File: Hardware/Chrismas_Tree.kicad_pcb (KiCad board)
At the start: 2 copper layers, 264.4 x 368.3 mm, 213 parts, among them J1 DNP, J2 USB_B, Q1 2N2222A, Q2 2N2222A, Q3 2N2222A, Q4 2N2222A, U1 PIC18F23K22

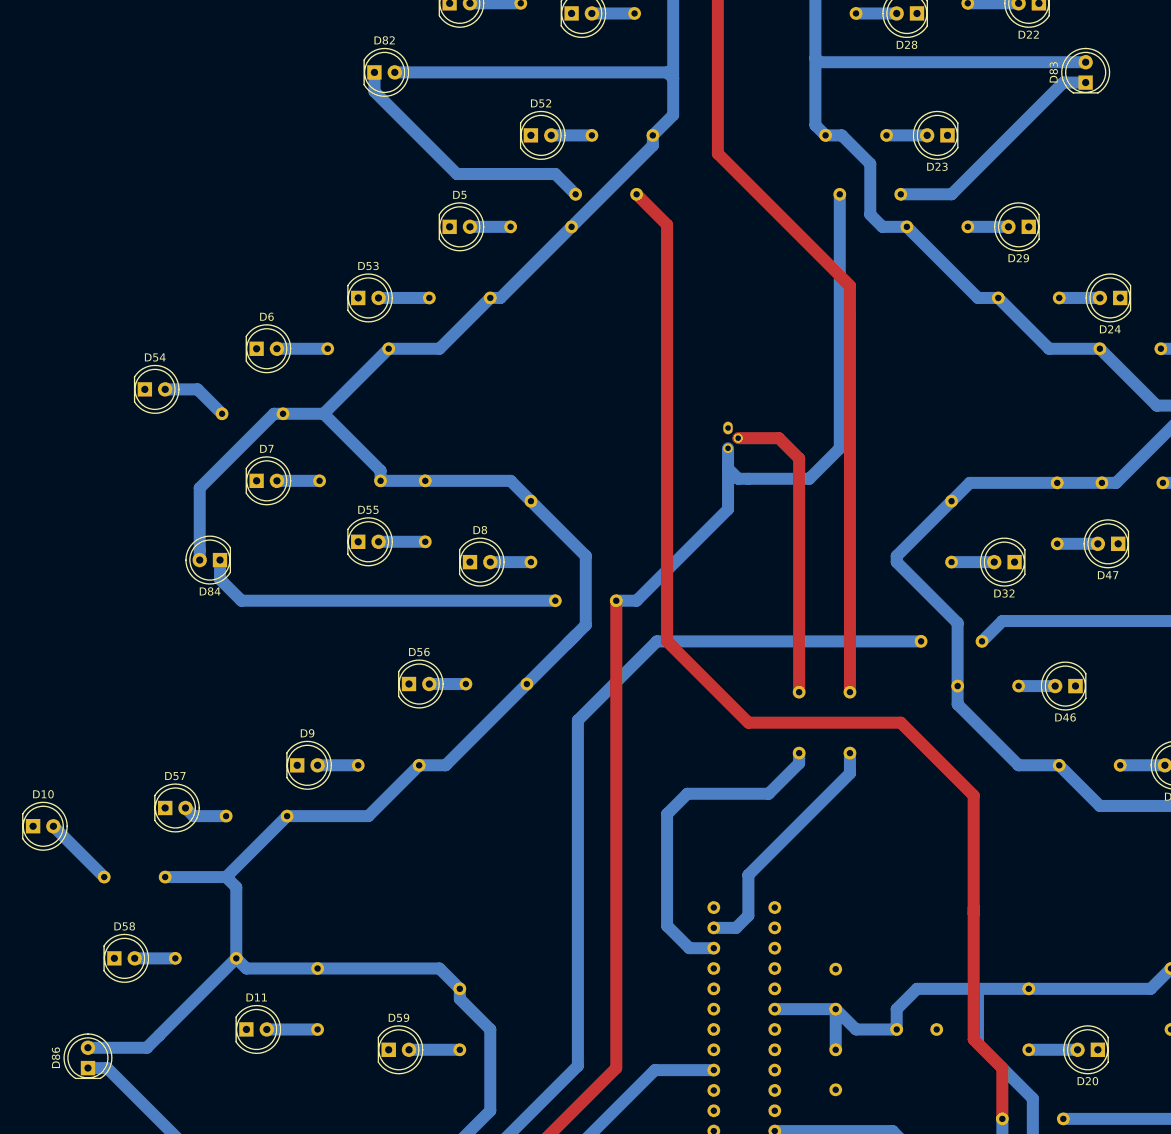
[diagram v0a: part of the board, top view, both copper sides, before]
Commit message: Turned rotated leds to have all them on the same axis (but trunk base ones).
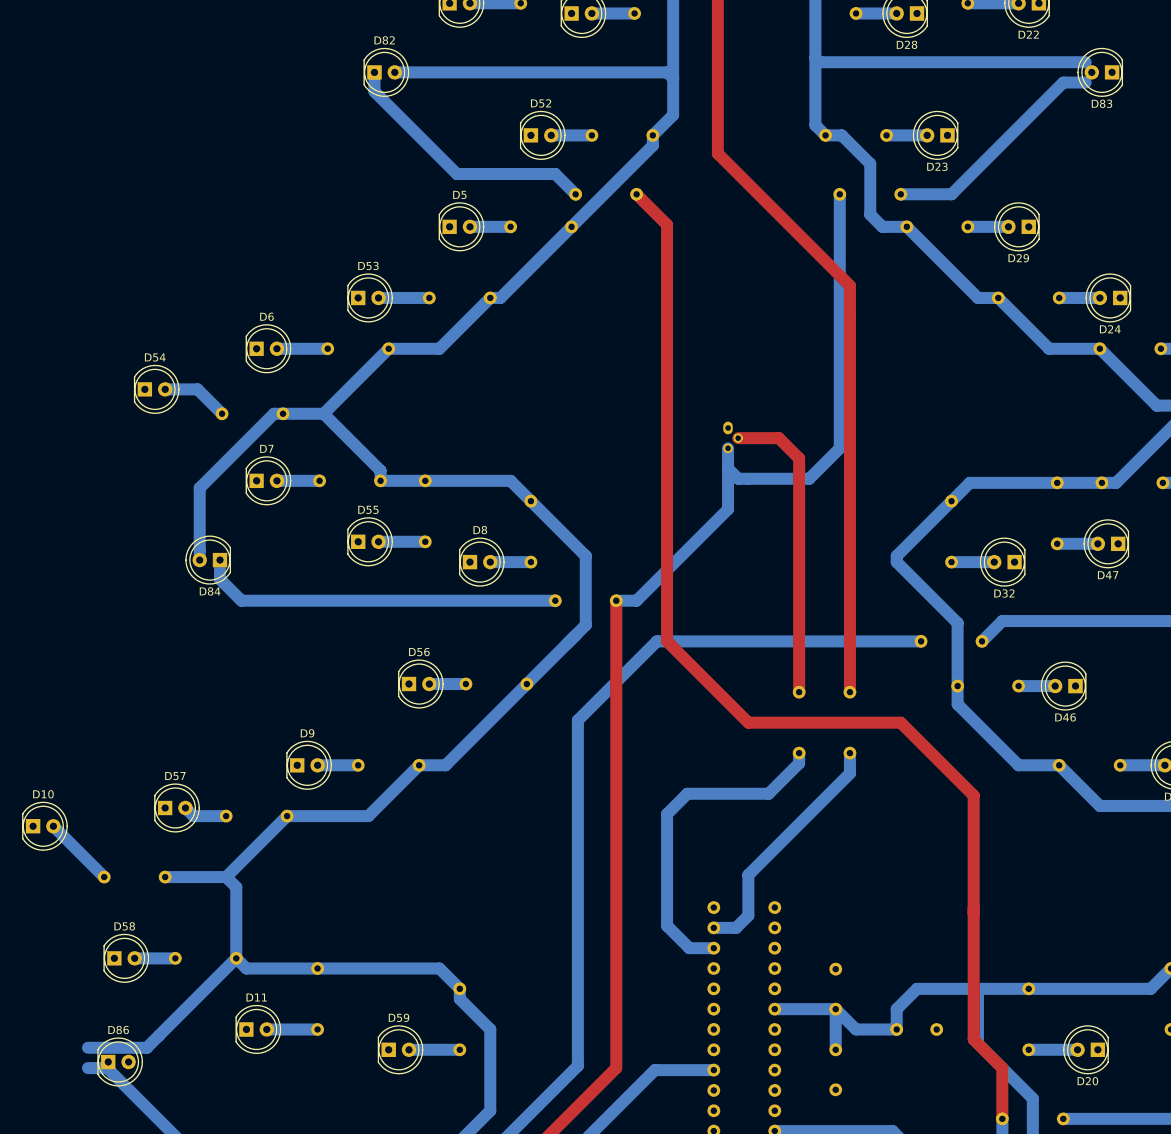
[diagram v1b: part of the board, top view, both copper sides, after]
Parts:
- moved D83 3.54 mm to (208.0, 127.0), turned to 180 degrees
- moved D86 2.65 mm to (82.5, 250.7), turned to 0 degrees
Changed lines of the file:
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@@
   (general
     (thickness 1.6)
-    (drawings 7)
+    (drawings 8)
     (tracks 514)
     (zones 0)
@@
   )
   (module LED_THT:LED_D5.0mm (layer F.Cu)
-    (at 80.01 251.46 90)
+    (at 82.55 250.698)
     (descr "LED, diameter 5.0mm, 2 pins, http://cdn-reichelt.de/documents/datenblatt/A500/LL-504BC2E-009.pdf")
     (tags "LED diameter 5.0mm 2 pins")
-    (fp_text reference D86 (at 1.27 -3.96 90) (layer F.SilkS)
+    (fp_text reference D86 (at 1.27 -3.96) (layer F.SilkS)
       (effects (font (size 1 1) (thickness 0.15)))
     )
-    (fp_text value Yellow (at 1.27 3.96 90) (layer F.Fab)
+    (fp_text value Yellow (at 1.27 3.96) (layer F.Fab)
       (effects (font (size 1 1) (thickness 0.15)))
     )
-    (fp_text user %R (at 1.25 0 90) (layer F.Fab)
+    (fp_text user %R (at 1.25 0) (layer F.Fab)
       (effects (font (size 0.8 0.8) (thickness 0.2)))
     )
@@
     (fp_arc (start 1.27 0) (end -1.29 -1.54483) (angle 148.9) (layer F.SilkS) (width 0.12))
     (fp_arc (start 1.27 0) (end -1.23 -1.469694) (angle 299.1) (layer F.Fab) (width 0.1))
-    (pad 2 thru_hole circle (at 2.54 0 90) (size 1.8 1.8) (drill 0.9) (layers *.Cu *.Mask)
+    (pad 2 thru_hole circle (at 2.54 0) (size 1.8 1.8) (drill 0.9) (layers *.Cu *.Mask)
       (net 83 +5V))
-    (pad 1 thru_hole rect (at 0 0 90) (size 1.8 1.8) (drill 0.9) (layers *.Cu *.Mask)
+    (pad 1 thru_hole rect (at 0 0) (size 1.8 1.8) (drill 0.9) (layers *.Cu *.Mask)
       (net 110 "Net-(D86-Pad1)"))
     (model ${KISYS3DMOD}/LED_THT.3dshapes/LED_D5.0mm.wrl
@@
   )
   (module LED_THT:LED_D5.0mm (layer F.Cu)
-    (at 204.724 128.27 90)
+    (at 208.026 127 180)
     (descr "LED, diameter 5.0mm, 2 pins, http://cdn-reichelt.de/documents/datenblatt/A500/LL-504BC2E-009.pdf")
     (tags "LED diameter 5.0mm 2 pins")
-    (fp_text reference D83 (at 1.27 -3.96 90) (layer F.SilkS)
+    (fp_text reference D83 (at 1.27 -3.96) (layer F.SilkS)
       (effects (font (size 1 1) (thickness 0.15)))
     )
-    (fp_text value Red (at 1.27 3.96 90) (layer F.Fab)
+    (fp_text value Red (at 1.27 3.96) (layer F.Fab)
       (effects (font (size 1 1) (thickness 0.15)))
     )
-    (fp_text user %R (at 1.25 0 90) (layer F.Fab)
+    (fp_text user %R (at 1.25 0) (layer F.Fab)
       (effects (font (size 0.8 0.8) (thickness 0.2)))
     )
@@
     (fp_arc (start 1.27 0) (end -1.29 -1.54483) (angle 148.9) (layer F.SilkS) (width 0.12))
     (fp_arc (start 1.27 0) (end -1.23 -1.469694) (angle 299.1) (layer F.Fab) (width 0.1))
-    (pad 2 thru_hole circle (at 2.54 0 90) (size 1.8 1.8) (drill 0.9) (layers *.Cu *.Mask)
+    (pad 2 thru_hole circle (at 2.54 0 180) (size 1.8 1.8) (drill 0.9) (layers *.Cu *.Mask)
       (net 83 +5V))
-    (pad 1 thru_hole rect (at 0 0 90) (size 1.8 1.8) (drill 0.9) (layers *.Cu *.Mask)
+    (pad 1 thru_hole rect (at 0 0 180) (size 1.8 1.8) (drill 0.9) (layers *.Cu *.Mask)
       (net 107 "Net-(D83-Pad1)"))
     (model ${KISYS3DMOD}/LED_THT.3dshapes/LED_D5.0mm.wrl
@@
     )
   )
+  (dimension 131 (width 0.12) (layer F.SilkS)
+    (gr_text "131,000 mm" (at 227.45 24.34) (layer F.SilkS)
+      (effects (font (size 1 1) (thickness 0.15)))
+    )
+    (feature1 (pts (xy 292.95 384.61) (xy 292.95 25.023579)))
+    (feature2 (pts (xy 161.95 384.61) (xy 161.95 25.023579)))
+    (crossbar (pts (xy 161.95 25.61) (xy 292.95 25.61)))
+    (arrow1a (pts (xy 292.95 25.61) (xy 291.823496 26.196421)))
+    (arrow1b (pts (xy 292.95 25.61) (xy 291.823496 25.023579)))
+    (arrow2a (pts (xy 161.95 25.61) (xy 163.076504 26.196421)))
+    (arrow2b (pts (xy 161.95 25.61) (xy 163.076504 25.023579)))
+  )
   (gr_text 11/2019 (at 262.89 388.62) (layer F.Mask)
     (effects (font (size 1 1) (thickness 0.15)))
@@
     (polygon
       (pts
-        (xy 28.702 25.654) (xy 293.116 25.654) (xy 293.116 393.954) (xy 28.702 393.954)
+        (xy 293.116 393.954) (xy 28.702 393.954) (xy 28.702 25.654) (xy 293.116 25.654)
       )
     )

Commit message: Replaced tree foliage through-hole resistors by SMD ones.
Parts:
- R1, R10, R11, R12, R13, R14, R15, R16, R17, R18, R19, R2, R20, R21, R22, R23, R24, R25, R26, R27, R28, R29, R3, R30, R31, R32, R33, R34, R35, R36, R37, R38, R39, R4, R40, R41, R42, R43, R44, R45, R46, R47, R48, R49, R5, R50, R51, R52, R53, R54, R55, R56, R57, R58, R59, R6, R60, R61, R62, R63, R64, R65, R66, R67, R68, R7, R8, R9: footprint Resistor_THT:R_Axial_DIN0207_L6.3mm_D2.5mm_P7.62mm_Horizontal -> Resistor_SMD:R_1206_3216Metric_Pad1.42x1.75mm_HandSolder
- moved R10 9.95 mm to (82.0, 221.2)
- moved R34 9.59 mm to (241.8, 221.5)
- moved R54 8.95 mm to (96.0, 166.6)
- moved R48 8.62 mm to (226.6, 166.6)
- moved R62 8.10 mm to (275.9, 292.4)
- moved R38 7.88 mm to (45.9, 292.4)
- moved R8 7.69 mm to (136.4, 188.2), turned to 180 degrees
- moved R32 7.66 mm to (187.2, 188.2), turned to 0 degrees
- moved R28 7.66 mm to (175.3, 119.6), turned to 0 degrees
- moved R12 7.66 mm to (115.0, 264.4)
- moved R59 7.63 mm to (126.2, 249.2), turned to 180 degrees
- moved R4 7.62 mm to (148.6, 119.6), turned to 180 degrees
- moved R20 7.62 mm to (197.6, 249.2), turned to 0 degrees
- moved R36 7.40 mm to (208.8, 264.4)
- moved R53 7.40 mm to (122.9, 155.2)
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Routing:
- net +5V: track 1804.1 -> 2168.2 mm
- net Net-(D83-Pad1): track 28.9 -> 34.1 mm
- net Net-(D10-Pad2): track 8.98 -> 4.83 mm
- net Net-(D34-Pad2): track 8.41 -> 4.32 mm
- net Net-(D54-Pad2): track 8.37 -> 4.83 mm
- net Net-(D48-Pad2): track 8.21 -> 5.12 mm
- net Net-(D62-Pad2): track 7.67 -> 5.08 mm
- net Net-(D38-Pad2): track 7.42 -> 5.08 mm
- net Net-(D59-Pad2): track 6.35 -> 4.57 mm
- net Net-(D20-Pad2): track 6.10 -> 4.57 mm
- net Net-(D12-Pad2): track 5.84 -> 4.32 mm
- net Net-(D45-Pad2): track 5.75 -> 4.39 mm
- net Net-(D4-Pad2): track 5.33 -> 4.06 mm
- net Net-(D53-Pad2): track 6.35 -> 5.08 mm
- net Net-(D37-Pad2): track 6.35 -> 5.33 mm
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
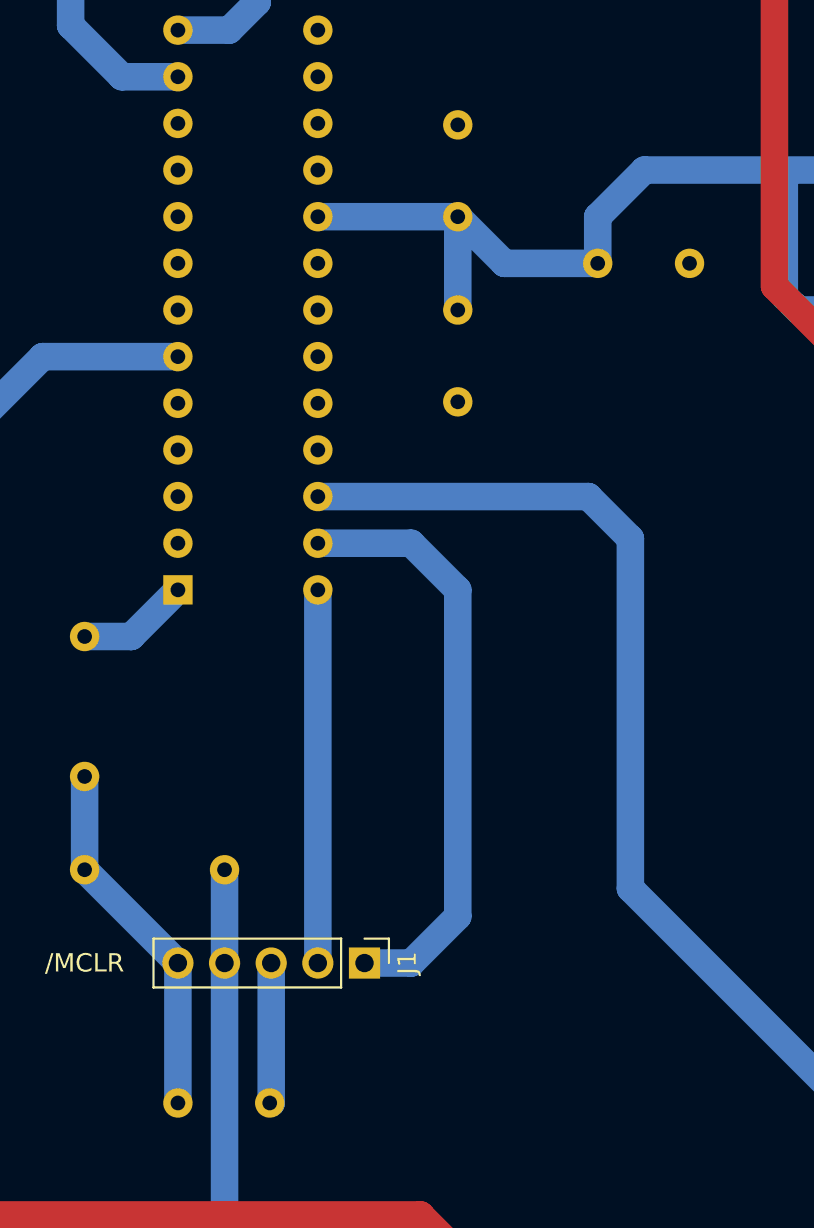
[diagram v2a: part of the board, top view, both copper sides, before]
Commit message: Replaced though-hole capacitors by SMD ones.
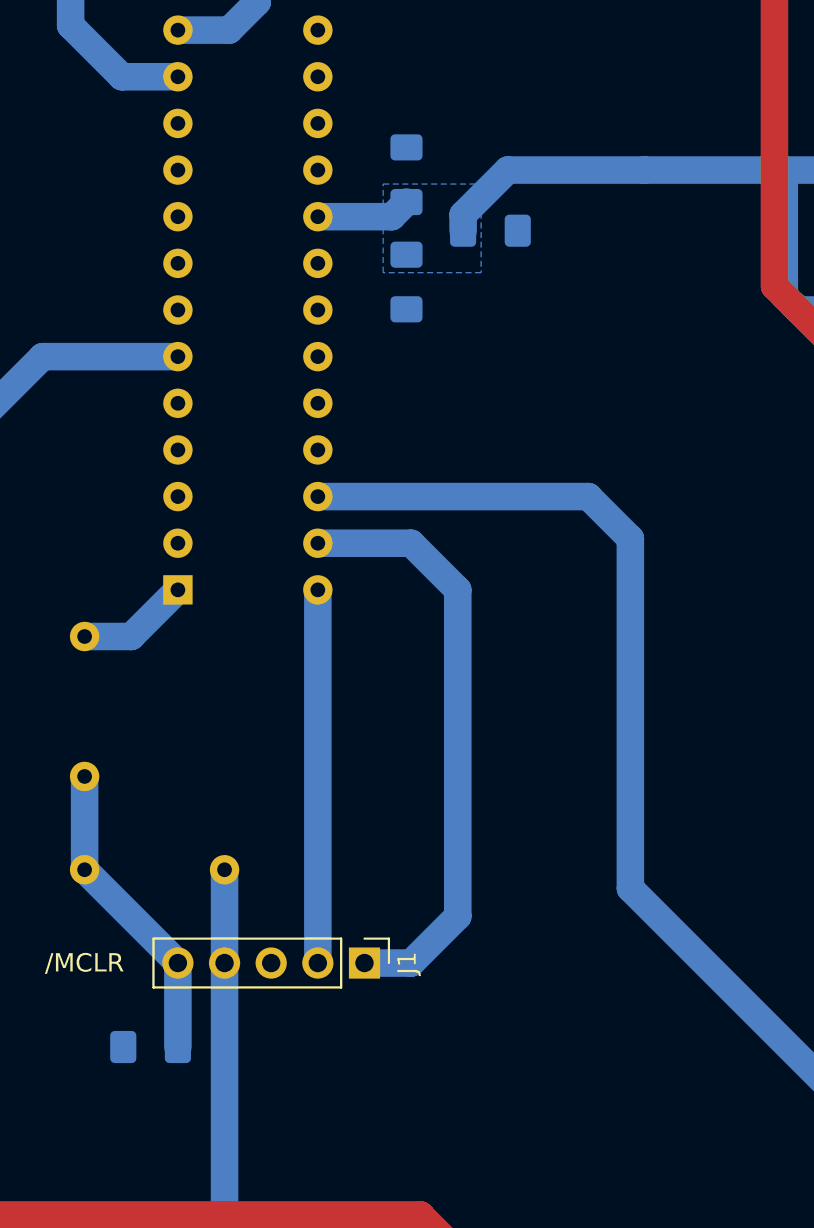
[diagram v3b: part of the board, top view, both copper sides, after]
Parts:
- C1, C2, C3, C4: footprint Capacitor_THT:C_Disc_D5.0mm_W2.5mm_P5.00mm -> Capacitor_SMD:C_1206_3216Metric_Pad1.42x1.75mm_HandSolder
- moved C3 6.11 mm to (175.3, 244.9)
- moved C1 3.61 mm to (170.7, 241.8)
- moved C4 3.39 mm to (156.8, 289.3), turned to 180 degrees
- moved C2 3.18 mm to (170.7, 247.7)
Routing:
- net +5V: track 2168.2 -> 2157.6 mm
- net GND: track 20.6 -> 12.9 mm
- net Net-(C4-Pad1): track 19.9 -> 16.8 mm
- added copper zone on B.Cu, net +5V

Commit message: Replaced through-hole transistors by SMD ones.
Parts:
- Q1, Q2, Q3, Q4: value 2N2222A -> DMG3414U; footprint Package_TO_SOT_THT:TO-18-3 -> Package_TO_SOT_SMD:SOT-23
- R100, R101, R96, R99: value 820 -> 10K; footprint Resistor_THT:R_Axial_DIN0207_L6.3mm_D2.5mm_P7.62mm_Horizontal -> Resistor_SMD:R_1206_3216Metric_Pad1.42x1.75mm_HandSolder
- moved Q1 167.7 mm to (165.9, 219.2)
- moved R101 44.2 mm to (181.9, 260.8), turned to 90 degrees
- moved Q2 43.5 mm to (153.2, 214.4), turned to 90 degrees
- moved Q4 38.5 mm to (186.9, 258.4), turned to 0 degrees
- moved R96 21.2 mm to (168.4, 224.5), turned to 180 degrees
- moved R100 20.1 mm to (155.7, 219.7), turned to 180 degrees
- moved R99 10.8 mm to (134.1, 280.9), turned to 270 degrees
- moved Q3 7.33 mm to (128.5, 283.5), turned to 180 degrees
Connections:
- Q1 pad 1: GND -> Net-(Q1-Pad1)
- Q1 pad 2: Net-(Q1-Pad2) -> GND
- Q2 pad 1: GND -> Net-(Q2-Pad1)
- Q2 pad 2: Net-(Q2-Pad2) -> GND
- Q3 pad 1: GND -> Net-(Q3-Pad1)
- Q3 pad 2: Net-(Q3-Pad2) -> GND
- Q4 pad 1: GND -> Net-(Q4-Pad1)
- Q4 pad 2: Net-(Q4-Pad2) -> GND
- R100 pad 1: Net-(Q2-Pad2) -> GND
- R100 pad 2: Net-(R100-Pad2) -> Net-(Q2-Pad1)
- R101 pad 1: Net-(Q4-Pad2) -> GND
- R101 pad 2: Net-(R101-Pad2) -> Net-(Q4-Pad1)
- R96 pad 1: Net-(Q1-Pad2) -> GND
- R96 pad 2: Net-(R96-Pad2) -> Net-(Q1-Pad1)
- R99 pad 1: Net-(R99-Pad1) -> GND
- R99 pad 2: Net-(Q3-Pad2) -> Net-(Q3-Pad1)
- U1 pad 12: Net-(R100-Pad2) -> Net-(Q2-Pad1)
- U1 pad 13: Net-(R96-Pad2) -> Net-(Q1-Pad1)
- U1 pad 26: Net-(R101-Pad2) -> Net-(Q4-Pad1)
- U1 pad 6: Net-(R99-Pad1) -> Net-(Q3-Pad1)
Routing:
- net Net-(Q1-Pad2): track 166.5 -> 0.00 mm
- net Net-(D92-Pad1): track 31.2 -> 194.7 mm, vias 0 -> 1
- net Net-(R101-Pad2): track 60.4 -> 0.00 mm
- net Net-(Q3-Pad1): track 0.00 -> 54.7 mm
- net Net-(R99-Pad1): track 51.6 -> 0.00 mm
- net Net-(R100-Pad2): track 41.4 -> 0.00 mm
- net Net-(Q2-Pad2): track 37.9 -> 0.00 mm
- net Net-(R96-Pad2): track 30.5 -> 0.00 mm
- net Net-(Q2-Pad1): track 0.00 -> 28.8 mm
- net Net-(Q4-Pad1): track 0.00 -> 20.1 mm
- net Net-(Q1-Pad1): track 0.00 -> 19.3 mm
- net Net-(Q4-Pad2): track 6.88 -> 0.00 mm
- net Net-(Q4-Pad3): track 211.7 -> 218.3 mm
- net GND: track 12.9 -> 6.88 mm
- net Net-(Q3-Pad2): track 5.08 -> 0.00 mm
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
